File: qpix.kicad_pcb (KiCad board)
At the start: 4 copper layers, 82.6 x 92.8 mm, 112 parts, among them J1 Conn_01x40, J10 VC, J11 Conn_Coaxial_Power, J13 DigReset, J2 Conn_01x09, J3 Conn_02x03, J4 Conn_02x03, J5 SPI, J6 Conn_02x03, J7 Conn_Coaxial, J8 Conn_02x03, J9 Conn_Coaxial_Power, Q1 AO7400, Q2 AO7400, Q3 AO7400, Q4 AO7400, U1 qpix_digital, U2 TPS73101DBV, U3 9DMV0141AKILF, U4 DS90C401M_NOPB

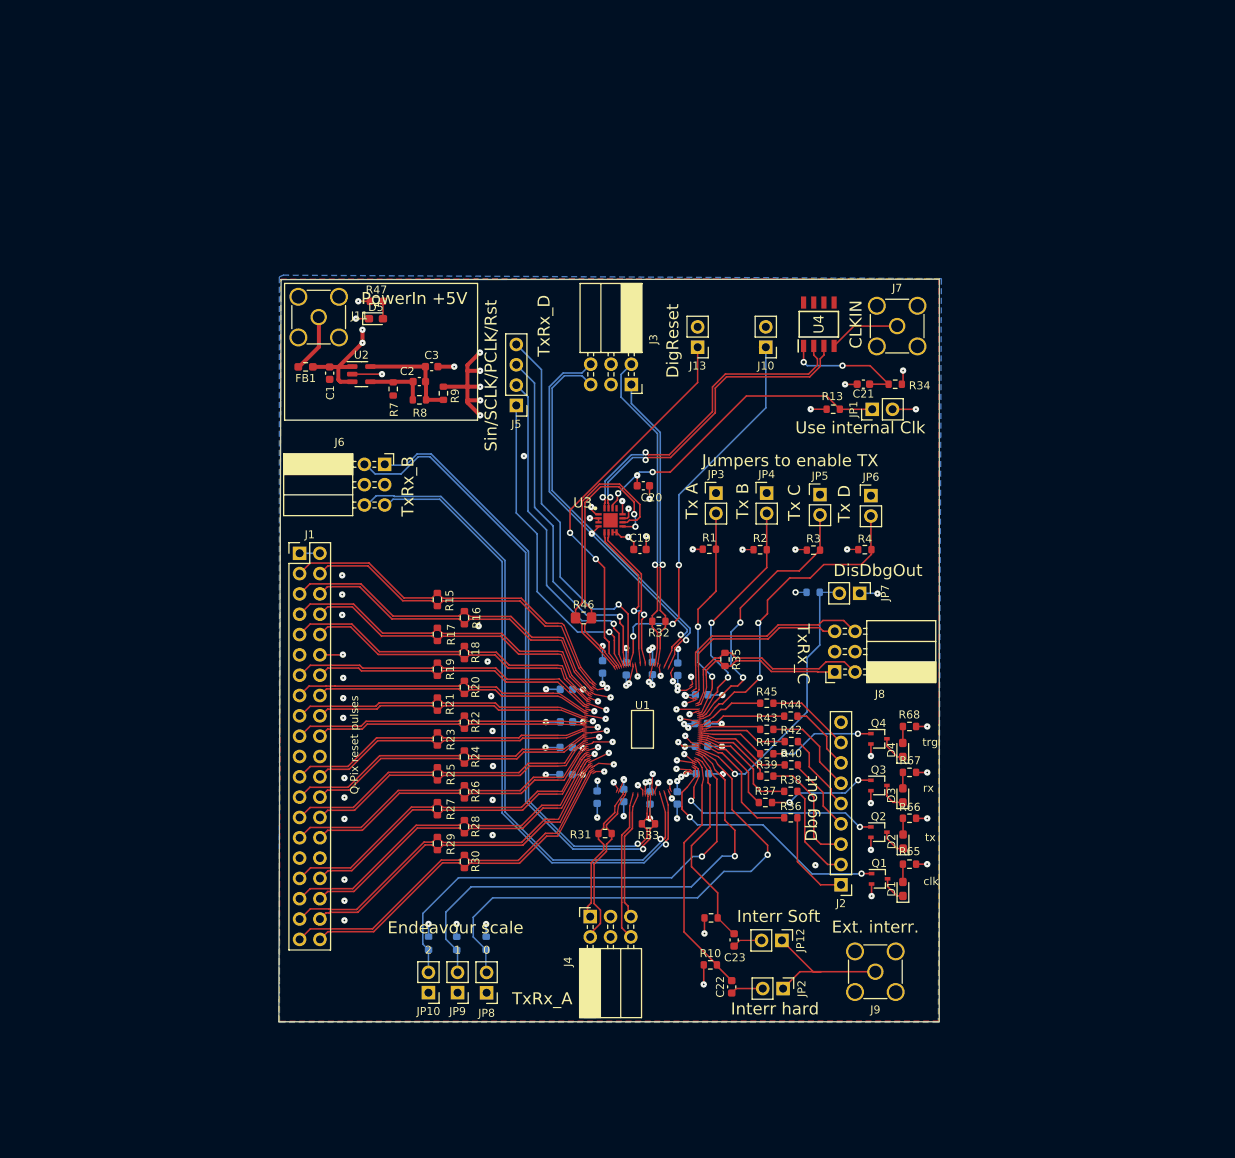
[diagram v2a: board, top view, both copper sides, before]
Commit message: lvds receiver/driver added for every endeavour port along with 3.3V power supply
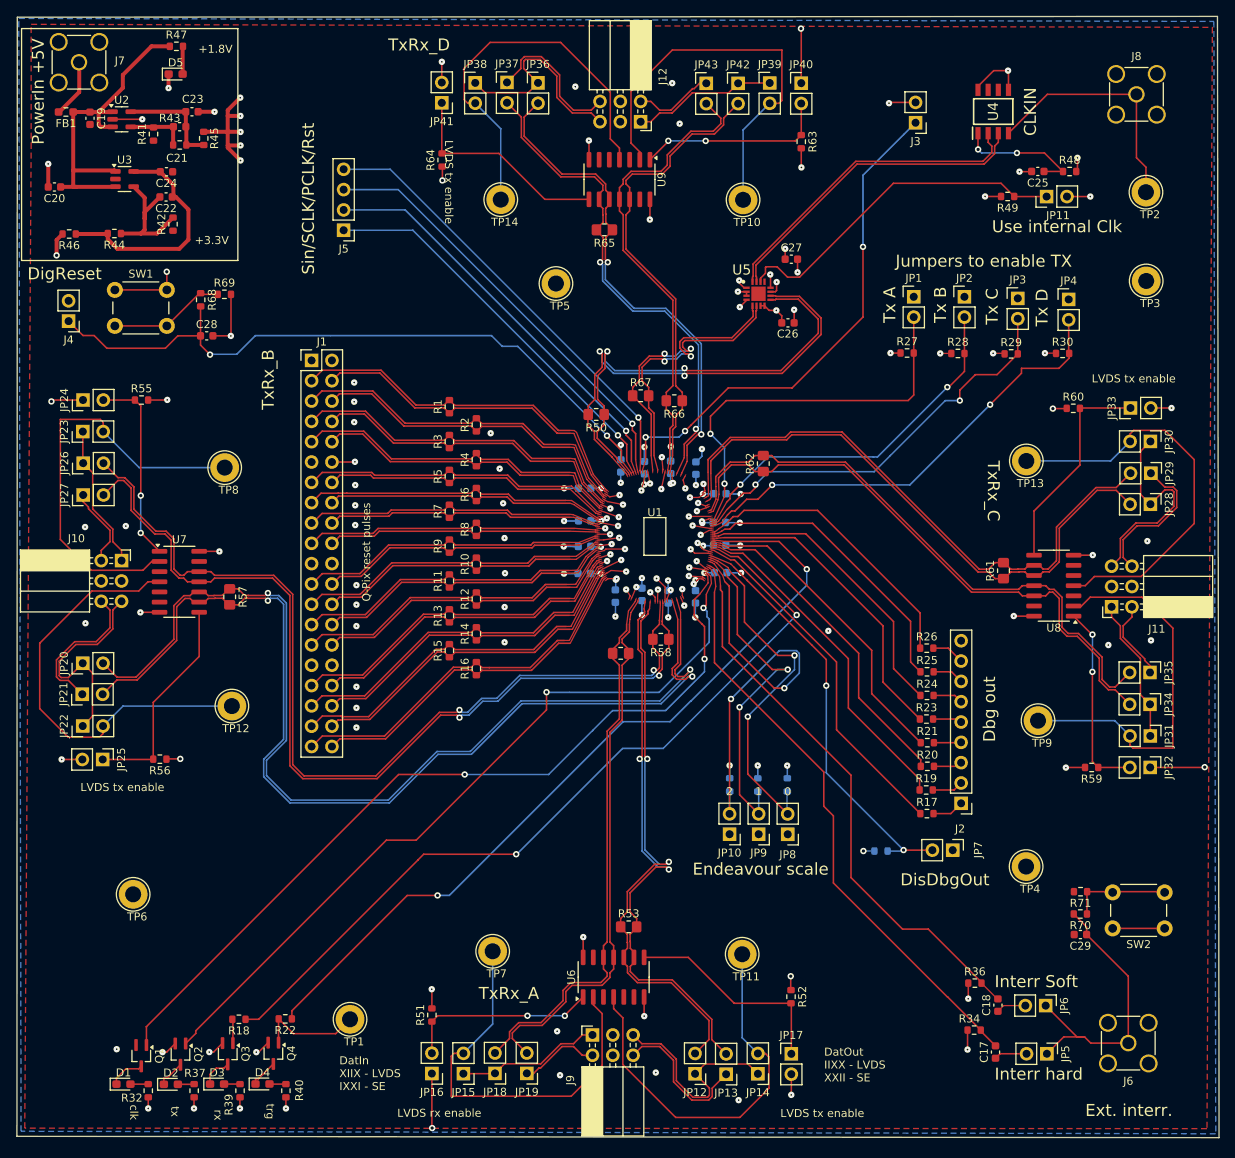
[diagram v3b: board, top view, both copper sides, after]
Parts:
- removed the J3 at (139.3, 62.6)
- removed the J4 at (134.2, 129.1)
- removed the J6 at (108.5, 72.6)
- removed the J8 at (164.7, 98.5)
- removed the R31 at (136.0, 118.7)
- removed the R32 at (142.8, 92.2)
- removed the R33 at (141.4, 117.5)
- removed the R35 at (151.0, 97.0)
- added C20: 10uF, Capacitor_SMD:C_0603_1608Metric, F.Cu at (67.2, 37.9)
- added C22: 15pF, Capacitor_SMD:C_0603_1608Metric, F.Cu at (81.2, 39.1)
- added C24: 10uF, Capacitor_SMD:C_0603_1608Metric, F.Cu at (81.2, 36.0)
- added C28: C, Capacitor_SMD:C_0603_1608Metric, F.Cu at (86.2, 56.5)
- added C29: C, Capacitor_SMD:C_0603_1608Metric, F.Cu at (195.4, 131.3)
- added J10: Conn_02x03, Connector_PinSocket_2.54mm:PinSocket_2x03_P2.54mm_Horizontal, F.Cu at (75.6, 84.6)
- added J11: Conn_02x03, Connector_PinSocket_2.54mm:PinSocket_2x03_P2.54mm_Horizontal, F.Cu at (199.3, 90.4)
- added J12: Conn_02x03, Connector_PinSocket_2.54mm:PinSocket_2x03_P2.54mm_Horizontal, F.Cu at (140.5, 29.7)
- added J9: Conn_02x03, Connector_PinSocket_2.54mm:PinSocket_2x03_P2.54mm_Horizontal, F.Cu at (134.5, 143.9)
- added JP12: Jumper_2_Open, Connector_PinHeader_2.54mm:PinHeader_1x02_P2.54mm_Vertical, F.Cu at (147.3, 148.7)
- added JP13: Jumper_2_Open, Connector_PinHeader_2.54mm:PinHeader_1x02_P2.54mm_Vertical, F.Cu at (151.2, 148.8)
- added JP14: Jumper_2_Bridged, Connector_PinHeader_2.54mm:PinHeader_1x02_P2.54mm_Vertical, F.Cu at (155.1, 148.7)
- added JP15: Jumper_2_Bridged, Connector_PinHeader_2.54mm:PinHeader_1x02_P2.54mm_Vertical, F.Cu at (118.3, 148.7)
- added JP16: Jumper_2_Open, Connector_PinHeader_2.54mm:PinHeader_1x02_P2.54mm_Vertical, F.Cu at (114.4, 148.7)
- added JP17: Jumper_2_Open, Connector_PinHeader_2.54mm:PinHeader_1x02_P2.54mm_Vertical, F.Cu at (159.3, 146.2)
- added JP18: Jumper_2_Open, Connector_PinHeader_2.54mm:PinHeader_1x02_P2.54mm_Vertical, F.Cu at (122.3, 148.7)
- added JP19: Jumper_2_Open, Connector_PinHeader_2.54mm:PinHeader_1x02_P2.54mm_Vertical, F.Cu at (126.2, 148.7)
- added JP20: Jumper_2_Open, Connector_PinHeader_2.54mm:PinHeader_1x02_P2.54mm_Vertical, F.Cu at (70.7, 97.4)
- added JP21: Jumper_2_Open, Connector_PinHeader_2.54mm:PinHeader_1x02_P2.54mm_Vertical, F.Cu at (70.7, 101.3)
- added JP22: Jumper_2_Bridged, Connector_PinHeader_2.54mm:PinHeader_1x02_P2.54mm_Vertical, F.Cu at (70.7, 105.3)
- added JP23: Jumper_2_Bridged, Connector_PinHeader_2.54mm:PinHeader_1x02_P2.54mm_Vertical, F.Cu at (70.8, 68.5)
- added JP24: Jumper_2_Open, Connector_PinHeader_2.54mm:PinHeader_1x02_P2.54mm_Vertical, F.Cu at (70.8, 64.5)
- added JP25: Jumper_2_Open, Connector_PinHeader_2.54mm:PinHeader_1x02_P2.54mm_Vertical, F.Cu at (73.2, 109.5)
- added JP26: Jumper_2_Open, Connector_PinHeader_2.54mm:PinHeader_1x02_P2.54mm_Vertical, F.Cu at (70.8, 72.4)
- added JP27: Jumper_2_Open, Connector_PinHeader_2.54mm:PinHeader_1x02_P2.54mm_Vertical, F.Cu at (70.8, 76.4)
- added JP28: Jumper_2_Open, Connector_PinHeader_2.54mm:PinHeader_1x02_P2.54mm_Vertical, F.Cu at (204.2, 77.5)
- added JP29: Jumper_2_Open, Connector_PinHeader_2.54mm:PinHeader_1x02_P2.54mm_Vertical, F.Cu at (204.3, 73.7)
- added JP30: Jumper_2_Bridged, Connector_PinHeader_2.54mm:PinHeader_1x02_P2.54mm_Vertical, F.Cu at (204.2, 69.7)
- added JP31: Jumper_2_Bridged, Connector_PinHeader_2.54mm:PinHeader_1x02_P2.54mm_Vertical, F.Cu at (204.2, 106.5)
- added JP32: Jumper_2_Open, Connector_PinHeader_2.54mm:PinHeader_1x02_P2.54mm_Vertical, F.Cu at (204.2, 110.5)
- added JP33: Jumper_2_Open, Connector_PinHeader_2.54mm:PinHeader_1x02_P2.54mm_Vertical, F.Cu at (201.7, 65.5)
- added JP34: Jumper_2_Open, Connector_PinHeader_2.54mm:PinHeader_1x02_P2.54mm_Vertical, F.Cu at (204.1, 102.6)
- added JP35: Jumper_2_Open, Connector_PinHeader_2.54mm:PinHeader_1x02_P2.54mm_Vertical, F.Cu at (204.1, 98.6)
- added JP36: Jumper_2_Open, Connector_PinHeader_2.54mm:PinHeader_1x02_P2.54mm_Vertical, F.Cu at (127.7, 24.9)
- added JP37: Jumper_2_Open, Connector_PinHeader_2.54mm:PinHeader_1x02_P2.54mm_Vertical, F.Cu at (123.8, 24.8)
- added JP38: Jumper_2_Bridged, Connector_PinHeader_2.54mm:PinHeader_1x02_P2.54mm_Vertical, F.Cu at (119.8, 24.9)
- added JP39: Jumper_2_Bridged, Connector_PinHeader_2.54mm:PinHeader_1x02_P2.54mm_Vertical, F.Cu at (156.6, 24.9)
- added JP40: Jumper_2_Open, Connector_PinHeader_2.54mm:PinHeader_1x02_P2.54mm_Vertical, F.Cu at (160.6, 24.9)
- added JP41: Jumper_2_Open, Connector_PinHeader_2.54mm:PinHeader_1x02_P2.54mm_Vertical, F.Cu at (115.6, 27.4)
- added JP42: Jumper_2_Open, Connector_PinHeader_2.54mm:PinHeader_1x02_P2.54mm_Vertical, F.Cu at (152.7, 24.9)
- added JP43: Jumper_2_Open, Connector_PinHeader_2.54mm:PinHeader_1x02_P2.54mm_Vertical, F.Cu at (148.7, 24.9)
- added R42: 56.2k, Resistor_SMD:R_0603_1608Metric, F.Cu at (82.0, 42.5)
- added R44: 28.0k, Resistor_SMD:R_0603_1608Metric, F.Cu at (74.7, 43.7)
- added R50: NC, Resistor_SMD:R_0805_2012Metric_Pad1.20x1.40mm_HandSolder, F.Cu at (134.9, 66.3)
- added R51: R_Small_US, Resistor_SMD:R_0603_1608Metric, F.Cu at (114.4, 141.4)
- added R52: R_Small_US, Resistor_SMD:R_0603_1608Metric, F.Cu at (159.3, 139.1)
- added R53: 100, Resistor_SMD:R_0805_2012Metric_Pad1.20x1.40mm_HandSolder, F.Cu at (139.0, 130.4)
- added R54: 100, Resistor_SMD:R_0805_2012Metric_Pad1.20x1.40mm_HandSolder, F.Cu at (138.0, 96.2)
- added R55: R_Small_US, Resistor_SMD:R_0603_1608Metric, F.Cu at (78.1, 64.5)
- added R56: R_Small_US, Resistor_SMD:R_0603_1608Metric, F.Cu at (80.4, 109.4)
- added R57: 100, Resistor_SMD:R_0805_2012Metric_Pad1.20x1.40mm_HandSolder, F.Cu at (89.1, 89.1)
- added R58: 100, Resistor_SMD:R_0805_2012Metric_Pad1.20x1.40mm_HandSolder, F.Cu at (143.0, 94.4)
- added R59: R_Small_US, Resistor_SMD:R_0603_1608Metric, F.Cu at (196.8, 110.5)
- added R60: R_Small_US, Resistor_SMD:R_0603_1608Metric, F.Cu at (194.6, 65.6)
- added R61: 100, Resistor_SMD:R_0805_2012Metric_Pad1.20x1.40mm_HandSolder, F.Cu at (185.8, 85.9)
- added R62: 100, Resistor_SMD:R_0805_2012Metric_Pad1.20x1.40mm_HandSolder, F.Cu at (155.8, 72.5)
- added R63: R_Small_US, Resistor_SMD:R_0603_1608Metric, F.Cu at (160.6, 32.2)
- added R64: R_Small_US, Resistor_SMD:R_0603_1608Metric, F.Cu at (115.7, 34.5)
- added R65: 100, Resistor_SMD:R_0805_2012Metric_Pad1.20x1.40mm_HandSolder, F.Cu at (136.0, 43.2)
- added R66: 100, Resistor_SMD:R_0805_2012Metric_Pad1.20x1.40mm_HandSolder, F.Cu at (144.7, 64.6)
- added R67: NC, Resistor_SMD:R_0805_2012Metric_Pad1.20x1.40mm_HandSolder, F.Cu at (140.5, 64.0)
- added R68: 10k, Resistor_SMD:R_0603_1608Metric, F.Cu at (85.5, 52.0)
- added R69: 10k, Resistor_SMD:R_0603_1608Metric, F.Cu at (88.4, 51.3)
- added R70: 10k, Resistor_SMD:R_0603_1608Metric, F.Cu at (195.4, 128.8)
- added R71: 10k, Resistor_SMD:R_0603_1608Metric, F.Cu at (195.5, 126.0)
- added SW1: SW_Push, Button_Switch_THT:SW_PUSH_6mm_H5mm, F.Cu at (74.8, 50.8)
- added SW2: SW_Push, Button_Switch_THT:SW_PUSH_6mm_H5mm, F.Cu at (206.0, 130.6)
- added TP1: TestInterr, TestPoint:TestPoint_Loop_D3.80mm_Drill2.0mm, F.Cu at (104.2, 141.9)
- added TP10: TestDatIn, TestPoint:TestPoint_Loop_D3.80mm_Drill2.0mm, F.Cu at (153.3, 39.5)
- added TP11: TestDatOut, TestPoint:TestPoint_Loop_D3.80mm_Drill2.0mm, F.Cu at (153.2, 133.8)
- added TP12: TestDatOut, TestPoint:TestPoint_Loop_D3.80mm_Drill2.0mm, F.Cu at (89.4, 102.8)
- added TP13: TestDatOut, TestPoint:TestPoint_Loop_D3.80mm_Drill2.0mm, F.Cu at (188.7, 72.1)
- added TP14: TestDatOut, TestPoint:TestPoint_Loop_D3.80mm_Drill2.0mm, F.Cu at (123.0, 39.5)
- added TP2: TestClkIn, TestPoint:TestPoint_Loop_D3.80mm_Drill2.0mm, F.Cu at (203.6, 38.5)
- added TP3: TestGnd, TestPoint:TestPoint_Loop_D3.80mm_Drill2.0mm, F.Cu at (203.7, 49.6)
- added TP4: TestGnd, TestPoint:TestPoint_Loop_D3.80mm_Drill2.0mm, F.Cu at (188.7, 122.8)
- added TP5: TestGnd, TestPoint:TestPoint_Loop_D3.80mm_Drill2.0mm, F.Cu at (129.9, 50.0)
- added TP6: TestGnd, TestPoint:TestPoint_Loop_D3.80mm_Drill2.0mm, F.Cu at (77.0, 126.3)
- added TP7: TestDatIn, TestPoint:TestPoint_Loop_D3.80mm_Drill2.0mm, F.Cu at (122.0, 133.4)
- added TP8: TestDatIn, TestPoint:TestPoint_Loop_D3.80mm_Drill2.0mm, F.Cu at (88.5, 73.0)
- added TP9: TestDatIn, TestPoint:TestPoint_Loop_D3.80mm_Drill2.0mm, F.Cu at (190.2, 104.6)
- added U3: TPS73101DBV, Package_TO_SOT_SMD:SOT-23-5, F.Cu at (76.0, 36.9)
- added U6: FIN1019M, Package_SO:SOIC-14_3.9x8.7mm_P1.27mm, F.Cu at (137.1, 136.7)
- added U7: FIN1019M, Package_SO:SOIC-14_3.9x8.7mm_P1.27mm, F.Cu at (82.8, 87.2)
- added U8: FIN1019M, Package_SO:SOIC-14_3.9x8.7mm_P1.27mm, F.Cu at (192.1, 87.7)
- added U9: FIN1019M, Package_SO:SOIC-14_3.9x8.7mm_P1.27mm, F.Cu at (137.8, 37.0)
- C10: renamed from C13; value locked -> 2uF
- C11: renamed from C14; value locked -> 2uF
- C12: renamed from C15; value locked -> 220nF
- C13: renamed from C16; value locked -> 220nF
- Q1, Q2, Q3, Q4: footprint Package_TO_SOT_SMD:SOT-323_SC-70 -> Package_TO_SOT_SMD:SOT-323_SC-70_Handsoldering
- R46: value NC -> 0; footprint Resistor_SMD:R_0805_2012Metric_Pad1.20x1.40mm_HandSolder -> Resistor_SMD:R_0603_1608Metric
- R47: value 220 -> 1k
- moved D1 100.4 mm to (75.8, 150.0), turned to 0 degrees
- moved R32 99.3 mm to (78.9, 150.9), turned to 90 degrees
- moved D2 96.4 mm to (81.8, 150.1), turned to 0 degrees
- moved R37 95.7 mm to (84.7, 150.9), turned to 90 degrees
- moved Q1 94.9 mm to (78.0, 146.5), turned to -90 degrees
- moved D3 93.0 mm to (87.5, 150.0), turned to 0 degrees
- moved R39 92.7 mm to (90.4, 150.9), turned to 90 degrees
- moved Q2 91.6 mm to (83.0, 146.3), turned to -90 degrees
- moved D4 90.3 mm to (93.2, 150.0), turned to 0 degrees
- moved R40 90.3 mm to (96.1, 150.9), turned to 90 degrees
- moved Q3 88.0 mm to (88.9, 146.2), turned to -90 degrees
- moved Q4 85.3 mm to (94.6, 146.2), turned to -90 degrees
- moved R46 80.2 mm to (69.0, 43.8), turned to 180 degrees
- moved J4 78.7 mm to (69.0, 54.7)
- moved R18 71.2 mm to (90.3, 141.9), turned to 180 degrees
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- renumbered C4 to C1, C17 to C14, C18 to C15, C24 to C16, C22 to C17, C23 to C18, C1 to C19, C5 to C2, C2 to C21, C3 to C23, C21 to C25, C19 to C26, C20 to C27, C6 to C3, C7 to C4, C8 to C5, C9 to C6, C10 to C7, C11 to C8, C12 to C9, J10 to J3, J13 to J4, J9 to J6, J11 to J7, J7 to J8, JP3 to JP1, JP1 to JP11, JP4 to JP2, JP5 to JP3, JP6 to JP4, JP2 to JP5, JP12 to JP6, R15 to R1, R24 to R10, R25 to R11, R26 to R12, R27 to R13, R28 to R14, R29 to R15, R30 to R16, R36 to R17, R37 to R18, R38 to R19, R16 to R2, R39 to R20, R40 to R21, R41 to R22, R42 to R23, R43 to R24, R44 to R25, R45 to R26, R1 to R27, R2 to R28, R3 to R29, R17 to R3, R4 to R30, R5 to R31, R65 to R32, R6 to R33, R10 to R34, R11 to R35, R14 to R36, R66 to R37, R12 to R38, R67 to R39, R18 to R4, R68 to R40, R7 to R41, R8 to R43, R9 to R45, R34 to R48, R13 to R49, R19 to R5, R20 to R6, R21 to R7, R22 to R8, R23 to R9, U3 to U5
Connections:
- R32 pad 1: +5V -> VCC
- R37 pad 1: +5V -> VCC
- R39 pad 1: +5V -> VCC
- R40 pad 1: +5V -> VCC
- R46 pad 1: CLKDIGIINN -> Net-(U3-OUT)
- R46 pad 2: CLKDIGIINP -> VCC
- U1 pad 101: /DataoutC_P -> DatoutC_P
- U1 pad 102: /DataoutC_N -> DatoutC_N
- U1 pad 106: /DataoutD_P -> DatoutD_P
- U1 pad 107: /DataoutD_N -> DatoutD_N
- U1 pad 109: /DatainD_P -> DatinD_P
- U1 pad 110: /DatainD_N -> DatinD_N
- U1 pad 51: /DatinA_P -> DatinA_P
- U1 pad 52: /DatinA_N -> DatinA_N
- U1 pad 53: /DatoutA_N -> DatoutA_N
- U1 pad 54: /DatoutA_P -> DatoutA_P
- U1 pad 57: /DatinB_P -> DatinB_P
- U1 pad 58: /DatinB_N -> DatinB_N
- U1 pad 61: /DatoutB_N -> DatoutB_N
- U1 pad 62: /DatoutB_P -> DatoutB_P
- U1 pad 97: /DatainC_P -> DatinC_P
- U1 pad 98: /DatainC_N -> DatinC_N
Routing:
- net DatoutB_N: track 0.00 -> 128.4 mm, vias 0 -> 2
- net DatoutB_P: track 0.00 -> 127.9 mm, vias 0 -> 2
- net DatinB_N: track 0.00 -> 118.1 mm, vias 0 -> 2
- net DatinB_P: track 0.00 -> 117.5 mm, vias 0 -> 2
- net Net-(U1-dbgInterr): track 8.57 -> 102.7 mm, vias 0 -> 2
- net Net-(U1-dbgRxValid): track 11.9 -> 103.7 mm, vias 0 -> 2
- net /DatoutB_N: track 82.3 -> 0.00 mm, vias 1 -> 0
- net /DatinB_N: track 82.3 -> 0.00 mm, vias 1 -> 0
- net /DatoutB_P: track 80.2 -> 0.00 mm, vias 1 -> 0
- net /DatinB_P: track 78.1 -> 0.00 mm, vias 1 -> 0
- net DatoutC_N: track 0.00 -> 74.8 mm
- net DatoutC_P: track 0.00 -> 74.7 mm
- net DatinC_N: track 0.00 -> 74.3 mm
- net DatinC_P: track 0.00 -> 74.1 mm
- net DatoutA_N: track 0.00 -> 71.3 mm, vias 0 -> 2
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- added copper zone on In2.Cu, net VCC
- removed copper zone on In2.Cu, net +5V
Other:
- board size 82.6 x 92.8 mm -> 150.3 x 140.2 mm
- board text added: "+1.8V"
- board text added: "+3.3V"
- board text added: "DatIn XIIX - LVDS IXXI - SE"
- board text added: "DatOut IIXX - LVDS XXII - SE"
- board text added: "LVDS rx enable"
- board text added: "LVDS tx enable"

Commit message: add mounting holes, make the board and the zones of rectangular shape, add sikscreen text
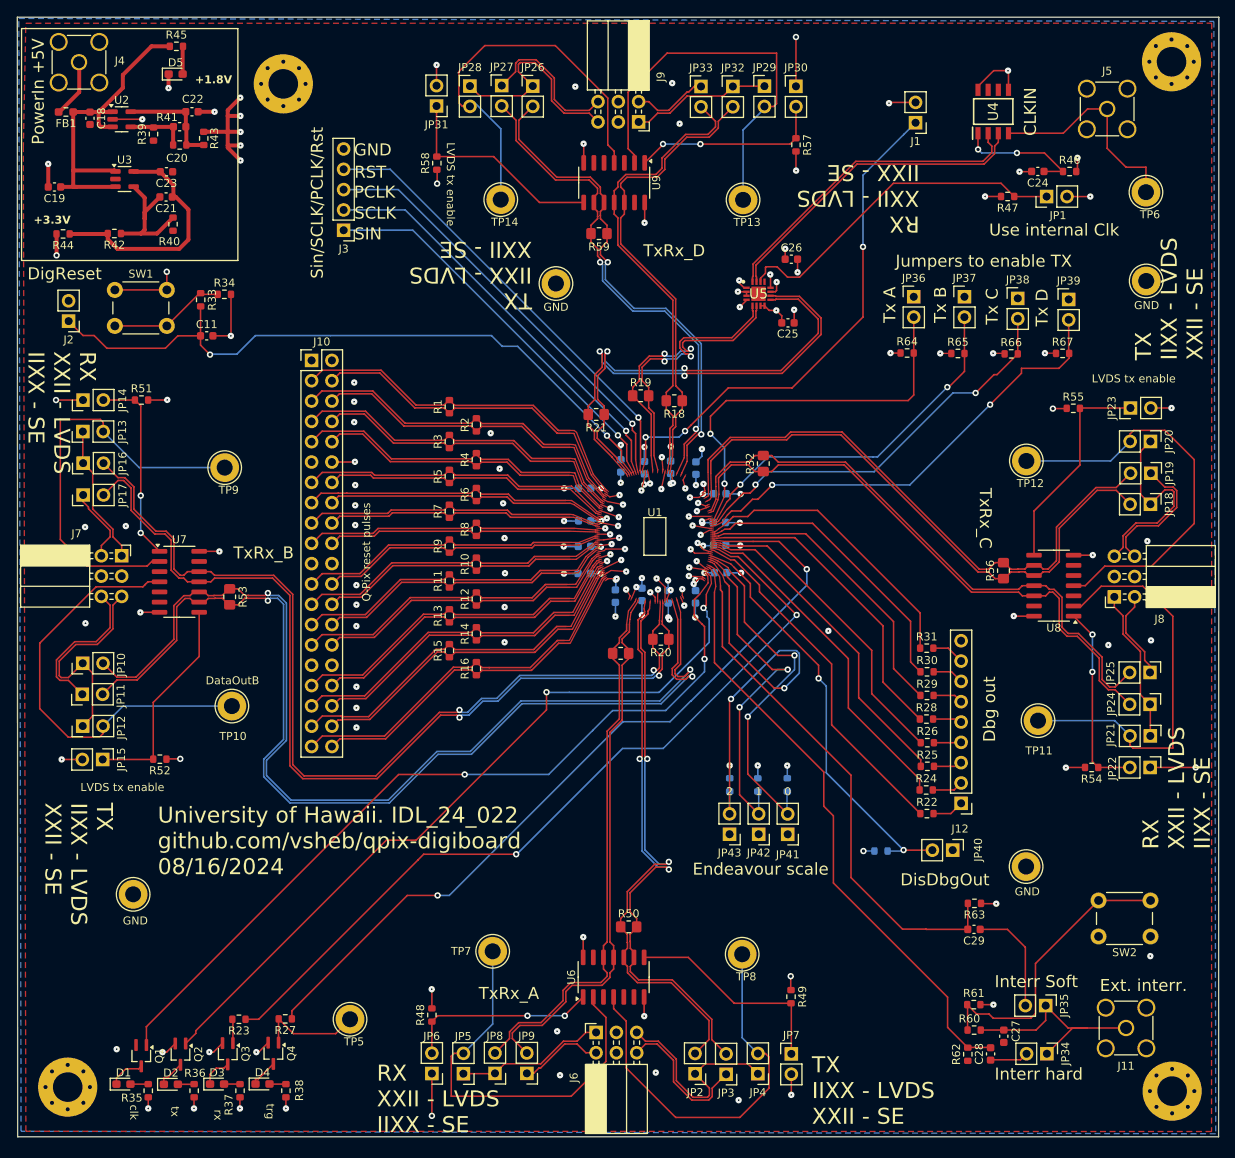
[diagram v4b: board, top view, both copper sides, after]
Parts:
- added H1: MountingHole_Pad, MountingHole:MountingHole_3.7mm_Pad_Via, F.Cu at (206.8, 22.2)
- added H2: MountingHole_Pad, MountingHole:MountingHole_3.7mm_Pad_Via, F.Cu at (95.8, 25.0)
- added H3: MountingHole_Pad, MountingHole:MountingHole_3.7mm_Pad_Via, F.Cu at (206.9, 150.9)
- added H4: MountingHole_Pad, MountingHole:MountingHole_3.7mm_Pad_Via, F.Cu at (68.9, 150.4)
- C27: renamed from C17; value 100nF -> C
- C29: value C -> 100nF
- J3: renamed from J5; footprint Connector_PinHeader_2.54mm:PinHeader_1x04_P2.54mm_Vertical -> Connector_PinHeader_2.54mm:PinHeader_1x05_P2.54mm_Vertical
- JP34: renamed from JP5; value (none) -> ~
- JP35: renamed from JP6; value (none) -> ~
- JP36: renamed from JP1; value (none) -> ~
- JP37: renamed from JP2; value (none) -> ~
- JP38: renamed from JP3; value (none) -> ~
- JP39: renamed from JP4; value (none) -> ~
- JP40: renamed from JP7; value (none) -> ~
- JP41: renamed from JP8; value (none) -> ~
- JP42: renamed from JP9; value (none) -> ~
- JP43: renamed from JP10; value (none) -> ~
- R40: renamed from R42; value 56.2k -> 30.1k
- R42: renamed from R44; value 28.0k -> 52.3k
- R60: renamed from R34; value 22k -> 10k
- R61: renamed from R36; value 22k -> 10k
- R62: renamed from R70; value 10k -> 22k
- R63: renamed from R71; value 10k -> 22k
- moved R62 22.5 mm to (181.4, 146.3), turned to 90 degrees
- moved R63 13.3 mm to (182.2, 127.4)
- moved C29 13.3 mm to (182.1, 130.7)
- moved C28 6.17 mm to (184.2, 146.3)
- moved J5 4.09 mm to (198.8, 28.1)
- moved R61 2.69 mm to (182.1, 140.1)
- moved C27 2.23 mm to (185.9, 144.1), turned to -90 degrees
- moved SW2 2.03 mm to (204.2, 131.6)
- moved J11 1.91 mm to (201.2, 143.0)
- moved J8 1.30 mm to (199.7, 89.1)
- moved R59 0.83 mm to (135.3, 43.7)
- moved R57 0.77 mm to (159.9, 32.6)
- moved JP29 0.77 mm to (155.9, 25.3)
- moved JP30 0.77 mm to (159.9, 25.3)
- moved U9 0.77 mm to (137.2, 37.4)
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- renumbered C28 to C11, C11 to C12, C12 to C13, C13 to C14, C14 to C15, C15 to C16, C16 to C17, C19 to C18, C20 to C19, C21 to C20, C22 to C21, C23 to C22, C24 to C23, C25 to C24, C26 to C25, C27 to C26, C18 to C28, J3 to J1, J1 to J10, J6 to J11, J2 to J12, J4 to J2, J7 to J4, J8 to J5, J9 to J6, J10 to J7, J11 to J8, J12 to J9, JP11 to JP1, JP20 to JP10, JP21 to JP11, JP22 to JP12, JP23 to JP13, JP24 to JP14, JP25 to JP15, JP26 to JP16, JP27 to JP17, JP28 to JP18, JP29 to JP19, JP12 to JP2, JP30 to JP20, JP31 to JP21, JP32 to JP22, JP33 to JP23, JP34 to JP24, JP35 to JP25, JP36 to JP26, JP37 to JP27, JP38 to JP28, JP39 to JP29, JP13 to JP3, JP40 to JP30, JP41 to JP31, JP42 to JP32, JP43 to JP33, JP14 to JP4, JP15 to JP5, JP16 to JP6, JP17 to JP7, JP18 to JP8, JP19 to JP9, R54 to R17, R66 to R18, R67 to R19, R58 to R20, R50 to R21, R17 to R22, R18 to R23, R19 to R24, R20 to R25, R21 to R26, R22 to R27, R23 to R28, R24 to R29, R25 to R30, R26 to R31, R62 to R32, R68 to R33, R69 to R34, R32 to R35, R37 to R36, R39 to R37, R40 to R38, R41 to R39, R43 to R41, R45 to R43, R46 to R44, R47 to R45, R48 to R46, R49 to R47, R51 to R48, R52 to R49, R53 to R50, R55 to R51, R56 to R52, R57 to R53, R59 to R54, R60 to R55, R61 to R56, R63 to R57, R64 to R58, R65 to R59, R27 to R64, R28 to R65, R29 to R66, R30 to R67, R31 to R68, R33 to R69, R35 to R70, R38 to R71, TP6 to TP1, TP12 to TP10, TP9 to TP11, TP13 to TP12, TP10 to TP13, TP3 to TP2, TP5 to TP3, TP1 to TP5, TP2 to TP6, TP11 to TP8, TP8 to TP9
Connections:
- C27 pad 1: Net-(JP5-B) (its old number) -> Net-(J11-In)
- C27 pad 2: extInterHard -> GND
- C28 pad 1: Net-(JP6-B) (its old number) -> Net-(JP34-B)
- C28 pad 2: extInterSoft -> extInterHard
- C29 pad 1: Net-(J6-In) -> Net-(JP35-B)
- C29 pad 2: GND -> extInterSoft
- J11 pad 1: Net-(J6-In) -> Net-(J11-In)
- JP34 pad 1: Net-(J6-In) -> Net-(J11-In)
- JP34 pad 2: Net-(JP5-B) (its old number) -> Net-(JP34-B)
- JP35 pad 1: Net-(J6-In) -> Net-(J11-In)
- JP35 pad 2: Net-(JP6-B) (its old number) -> Net-(JP35-B)
- R60 pad 1: GND -> Net-(R60-Pad1)
- R60 pad 2: extInterHard -> Net-(J11-In)
- R61 pad 1: GND -> Net-(R60-Pad1)
- R61 pad 2: extInterSoft -> GND
- R62 pad 1: Net-(R70-Pad1) -> GND
- R62 pad 2: Net-(J6-In) -> extInterHard
- R63 pad 1: Net-(R70-Pad1) -> GND
- R63 pad 2: GND -> extInterSoft
- SW2 pad 2: Net-(R70-Pad1) -> Net-(R60-Pad1)
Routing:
- net Net-(J6-In): track 36.8 -> 0.00 mm
- net Net-(R60-Pad1): track 0.00 -> 36.6 mm
- net Net-(J11-In): track 0.00 -> 28.1 mm
- net Net-(JP35-B): track 0.00 -> 13.9 mm
- net Net-(R70-Pad1): track 12.5 -> 0.00 mm
- net VDD: track 117.7 -> 111.2 mm, vias 58 -> 59
- net Net-(JP34-B): track 0.00 -> 4.82 mm
- net VCC: track 50.2 -> 45.9 mm
- net extInterSoft: track 71.1 -> 66.9 mm
- net Net-(JP5-B) (its old number): track 4.11 -> 0.00 mm
- net Net-(JP6-B) (its old number): track 3.73 -> 0.00 mm
- net /clkmux/CLK_DIN: track 30.7 -> 27.5 mm
- net Net-(JP21-B): track 48.4 -> 50.4 mm
- net extInterHard: track 74.8 -> 76.4 mm
- net /portC/Datout_IN_N: track 18.4 -> 17.0 mm
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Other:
- board size 150.3 x 140.2 mm -> 150.2 x 139.9 mm
- rule pad_to_mask_clearance: -0.5 -> -1
- board text added: "DataOutB"
- board text added: "GND"
- board text added: "PCLK"
- board text added: "RST"
- board text added: "RX XXII - LVDS IIXX - SE"
- board text added: "SCLK"
- board text added: "SIN"
- board text added: "TX IIXX - LVDS XXII - SE"
- board text added: "University of Hawaii. IDL_24_022 github.com/vsheb/qpix-digiboard 08/16/2024"
- board text removed: "DatIn XIIX - LVDS IXXI - SE"
- board text removed: "DatOut IIXX - LVDS XXII - SE"
- board text removed: "LVDS rx enable"
